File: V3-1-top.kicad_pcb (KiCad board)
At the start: 4 copper layers, 145 x 37.7 mm, 35 parts, among them IC1 MCP4451-103E_ST, IC2 MCP4451-103E_ST, IC3 MCP4451-103E_ST, J1 Conn_01x12_Female, J2 Conn_01x12_Female, J3 Conn_01x03_Male, J4 Conn_01x03_Male, J5 Conn_01x03_Male, J6 Conn_01x03_Male, J7 Conn_01x03_Male, J8 Conn_01x03_Male, U1 AMPLIFIER-PAM8403, U2 AMPLIFIER-PAM8403, U3 AMPLIFIER-PAM8403, U4 AMPLIFIER-PAM8403, U5 AMPLIFIER-PAM8403, U6 AMPLIFIER-PAM8403

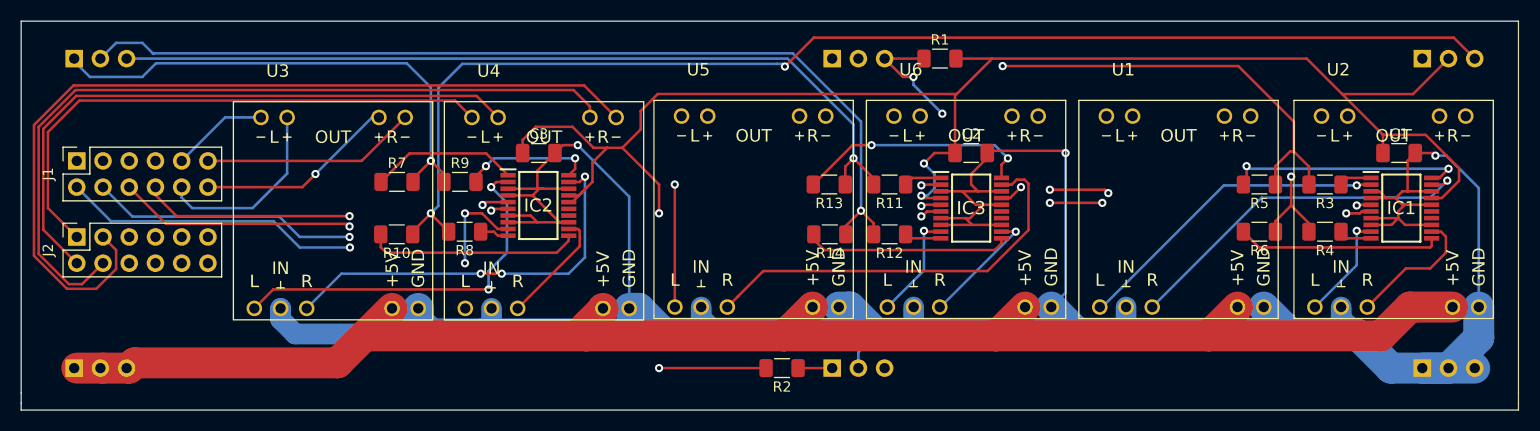
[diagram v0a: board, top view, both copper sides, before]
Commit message: Add bottom PCB WIP
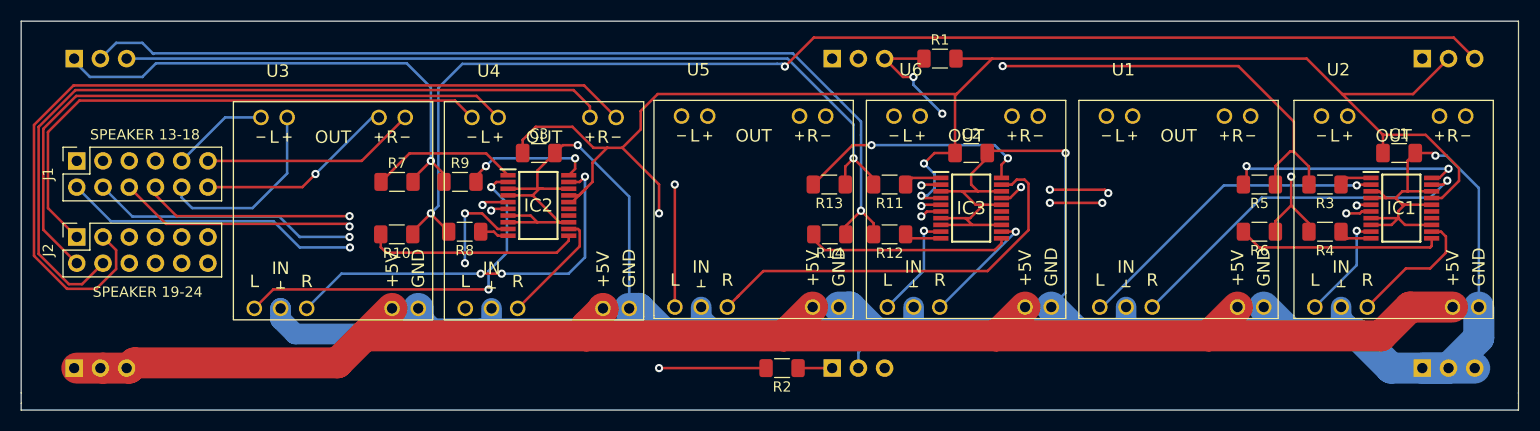
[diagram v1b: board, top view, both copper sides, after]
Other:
- board text added: "SPEAKER 13-18"
- board text added: "SPEAKER 19-24"

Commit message: Done BOT v3.1
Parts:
- removed ?: , HART:hart-logo-2000-2000dpi
- U1, U2, U3, U4, U5, U6: value AMPLIFIER-PAM8403 -> >VALUE
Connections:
- J7 pad 2: GND -> (no net)
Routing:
- net SPEAK22-: track 112.8 -> 132.2 mm
- net SPEAK13-: track 135.6 -> 116.6 mm
- net SPEAK14-: track 145.8 -> 127.8 mm, vias 0 -> 2
- net SPEAK14+: track 136.9 -> 119.1 mm, vias 1 -> 0
- net SPEAK13+: track 130.0 -> 114.1 mm
- net SCL1: track 127.6 -> 113.3 mm, vias 5 -> 7
- net SPEAK21+: track 89.9 -> 93.4 mm
- net SPEAK22+: track 103.2 -> 106.3 mm
- net GND: track 310.9 -> 309.3 mm
- net VDD: track 154.6 -> 153.2 mm
- net Net-(IC2-Pad9): track 14.0 -> 14.1 mm, vias 2 -> 1
- added copper zone on B.Cu, net GND
- added copper zone on F.Cu, net VDD

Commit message: Cleanup symbols and libraries and add separate submodule for kicad-libaries
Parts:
- U1, U2, U3, U4, U5, U6: value >VALUE -> AMPLIFIER-PAM8403
